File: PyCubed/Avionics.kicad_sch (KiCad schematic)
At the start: 37 parts, among them J19 F3311A7H121014E200, J8 Conn_01x09, U1 MAX706RESA, U2 ATSAMD51J19A-AU, U3 BMX160, Y1 32.768kHz

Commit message: PyCubed Schematic Finalized
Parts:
- added C61: 0.1uF, Capacitor_SMD:C_0603_1608Metric, symbol mainboard:C_Small
- added IC3: UA741IDT, SOIC127P600X175-8N, symbol SamacSys_Parts:UA741IDT
- added JP3, JP4: SolderJumper_2_Open, Jumper:SolderJumper-2_P1.3mm_Open_Pad1.0x1.5mm, symbol Jumper:SolderJumper_2_Open
- added R139, R140, R141, R143, R145: 10K, Resistor_SMD:R_0603_1608Metric, symbol Device:R_US
- added R144: ERA-8PEB6803V, ERA8P, symbol SamacSys_Parts:ERA-8PEB6803V
- added R30 (x2): 100K, Resistor_SMD:R_0603_1608Metric, symbol Device:R_US
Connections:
- net 3.3V: now also IC3.7 (VCC+), R139.1, R145.2
- net AIN5: now also C61.1, IC3.6 (OUTPUT), R144.2
- net GND: now also J19.MP1, J19.MP2, IC3.4 (VCC-), R140.2, R143.2; no longer J19.10
- net PB07: now also J19.12
- net PB09: now also J19.13
- net PB14: now also J19.14
- net RX: now also JP3.1 (A)
- net TX: now also JP4.1 (A)
- net at J19.11: now also JP3.2 (B)
- new net: C61.2, IC3.2 (INVERTING_INPUT), R144.1, R30.1
- new net: IC3.3 (NON-INVERTING_INPUT), R143.1, R30.1
- new net: J19.10, JP4.2 (B)
- new net: R139.2, R140.1, R30.2
- new net: R141.1, R145.1
- new net BAT_THERM: R141.2, R30.2

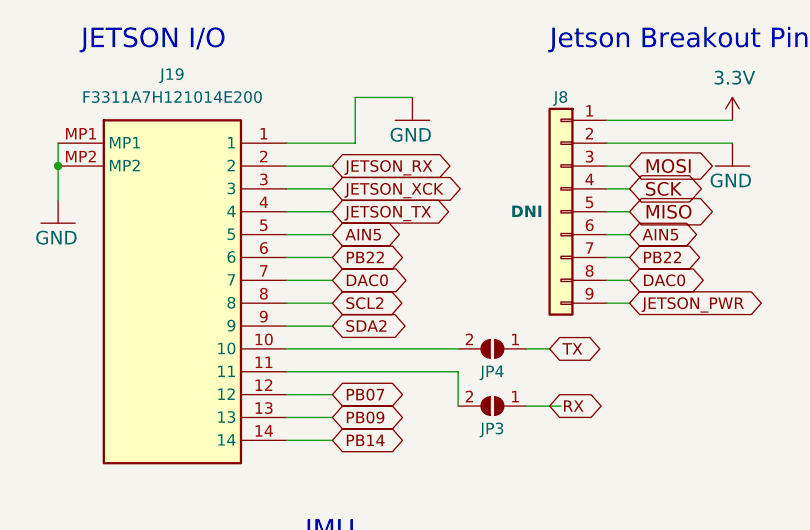
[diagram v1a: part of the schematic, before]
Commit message: PyCubed Interface Connectors Placed
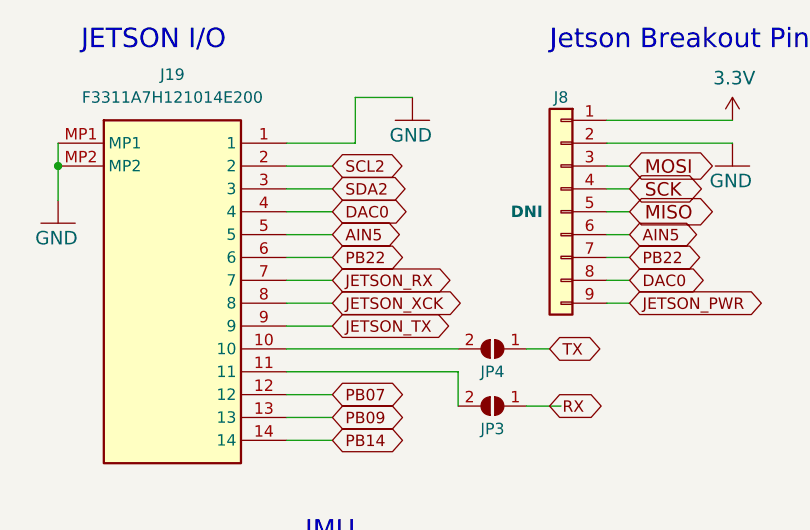
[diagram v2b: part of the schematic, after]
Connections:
- net DAC0: now also J19.4; no longer J19.7
- net JETSON_RX: now also J19.7; no longer J19.2
- net JETSON_TX: now also J19.9; no longer J19.4
- net JETSON_XCK: now also J19.8; no longer J19.3
- net SCL2: now also J19.2; no longer J19.8
- net SDA2: now also J19.3; no longer J19.9
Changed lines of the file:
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@@
     (effects (font (size 1.4986 1.4986)) (justify left bottom))
   )
-  (global_label "SDA2" (shape bidirectional) (at 218.44 57.15 0)
-    (effects (font (size 1.27 1.27)) (justify left))
-    (property "Intersheetrefs" "${INTERSHEET_REFS}" (at 218.44 57.15 0)
-      (effects (font (size 1.27 1.27)) hide)
-    )
-  )
   (global_label "ENAB_BURN1" (shape bidirectional) (at 127 161.29 0)
     (effects (font (size 1.27 1.27)) (justify left))
@@
     )
   )
+  (global_label "JETSON_XCK" (shape bidirectional) (at 218.44 54.61 0)
+    (effects (font (size 1.27 1.27)) (justify left))
+    (property "Intersheetrefs" "${INTERSHEET_REFS}" (at 218.44 54.61 0)
+      (effects (font (size 1.27 1.27)) hide)
+    )
+  )
   (global_label "PB09" (shape bidirectional) (at 127 130.81 0)
     (effects (font (size 1.27 1.27)) (justify left))
@@
     (effects (font (size 1.27 1.27)) (justify left))
     (property "Intersheetrefs" "${INTERSHEET_REFS}" (at 160.02 140.97 0)
+      (effects (font (size 1.27 1.27)) hide)
+    )
+  )
+  (global_label "SDA2" (shape bidirectional) (at 218.44 41.91 0)
+    (effects (font (size 1.27 1.27)) (justify left))
+    (property "Intersheetrefs" "${INTERSHEET_REFS}" (at 218.44 41.91 0)
       (effects (font (size 1.27 1.27)) hide)
     )
@@
     )
   )
-  (global_label "JETSON_TX" (shape bidirectional) (at 218.44 44.45 0)
-    (effects (font (size 1.27 1.27)) (justify left))
-    (property "Intersheetrefs" "${INTERSHEET_REFS}" (at 218.44 44.45 0)
-      (effects (font (size 1.27 1.27)) hide)
-    )
-  )
   (global_label "FLASH_IO2" (shape bidirectional) (at 88.9 130.81 180)
     (effects (font (size 1.27 1.27)) (justify right))
@@
     )
   )
+  (global_label "DAC0" (shape bidirectional) (at 218.44 44.45 0)
+    (effects (font (size 1.27 1.27)) (justify left))
+    (property "Intersheetrefs" "${INTERSHEET_REFS}" (at 218.44 44.45 0)
+      (effects (font (size 1.27 1.27)) hide)
+    )
+  )
   (global_label "JETSON_PWR" (shape bidirectional) (at 251.46 54.61 0)
     (effects (font (size 1.27 1.27)) (justify left))
@@
     (effects (font (size 1.27 1.27)) (justify right))
     (property "Intersheetrefs" "${INTERSHEET_REFS}" (at 90.17 172.72 0)
-      (effects (font (size 1.27 1.27)) hide)
-    )
-  )
-  (global_label "DAC0" (shape bidirectional) (at 218.44 52.07 0)
-    (effects (font (size 1.27 1.27)) (justify left))
-    (property "Intersheetrefs" "${INTERSHEET_REFS}" (at 218.44 52.07 0)
       (effects (font (size 1.27 1.27)) hide)
     )
@@
     )
   )
+  (global_label "SCL2" (shape bidirectional) (at 218.44 39.37 0)
+    (effects (font (size 1.27 1.27)) (justify left))
+    (property "Intersheetrefs" "${INTERSHEET_REFS}" (at 218.44 39.37 0)
+      (effects (font (size 1.27 1.27)) hide)
+    )
+  )
   (global_label "PB22" (shape bidirectional) (at 251.46 49.53 0)
     (effects (font (size 1.27 1.27)) (justify left))
@@
     )
   )
+  (global_label "JETSON_RX" (shape bidirectional) (at 218.44 52.07 0)
+    (effects (font (size 1.27 1.27)) (justify left))
+    (property "Intersheetrefs" "${INTERSHEET_REFS}" (at 218.44 52.07 0)
+      (effects (font (size 1.27 1.27)) hide)
+    )
+  )
   (global_label "AIN5" (shape bidirectional) (at 274.32 139.7 0)
     (effects (font (size 1.27 1.27)) (justify left))
@@
     )
   )
-  (global_label "JETSON_RX" (shape bidirectional) (at 218.44 39.37 0)
-    (effects (font (size 1.27 1.27)) (justify left))
-    (property "Intersheetrefs" "${INTERSHEET_REFS}" (at 218.44 39.37 0)
-      (effects (font (size 1.27 1.27)) hide)
-    )
-  )
   (global_label "VBUS_RESET" (shape output) (at 90.17 156.21 180)
     (effects (font (size 1.27 1.27)) (justify right))
@@
     )
   )
-  (global_label "JETSON_XCK" (shape bidirectional) (at 218.44 41.91 0)
-    (effects (font (size 1.27 1.27)) (justify left))
-    (property "Intersheetrefs" "${INTERSHEET_REFS}" (at 218.44 41.91 0)
-      (effects (font (size 1.27 1.27)) hide)
-    )
-  )
   (global_label "AIN5" (shape bidirectional) (at 251.46 46.99 0)
     (effects (font (size 1.27 1.27)) (justify left))
@@
     )
   )
-  (global_label "SCL2" (shape bidirectional) (at 218.44 54.61 0)
-    (effects (font (size 1.27 1.27)) (justify left))
-    (property "Intersheetrefs" "${INTERSHEET_REFS}" (at 218.44 54.61 0)
-      (effects (font (size 1.27 1.27)) hide)
-    )
-  )
   (global_label "PB07" (shape bidirectional) (at 127 125.73 0)
     (effects (font (size 1.27 1.27)) (justify left))
@@
       (effects (font (size 1.27 1.27)) hide)
     )
+  )
+  (global_label "JETSON_TX" (shape bidirectional) (at 218.44 57.15 0)
+    (effects (font (size 1.27 1.27)) (justify left))
+    (property "Intersheetrefs" "${INTERSHEET_REFS}" (at 218.44 57.15 0)
+      (effects (font (size 1.27 1.27)) hide)
+    )

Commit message: PyCubed Routing Done
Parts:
- removed J8: Conn_01x09, Connector_PinHeader_2.54mm:PinHeader_1x09_P2.54mm_Vertical, symbol Connector_Generic:Conn_01x09
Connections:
- net AIN5: no longer J19.5
- net BURN_RELAY_A: now also U2.10 (PB07); no longer U2.28 (PB15)
- net DAC0: now also J19.13; no longer J19.4
- net ENAB_BURN2: now also U2.12 (PB09); no longer U2.32 (PA15)
- net ENAB_BURN3: now also U2.13 (PA04); no longer U2.39 (PB16)
- net ENAB_BURN4: now also U2.27 (PB14); no longer U2.40 (PB17)
- net ENAB_IMU: now also U2.39 (PB16); no longer U2.9 (PB06)
- net ENAB_RF: now also U2.9 (PB06); no longer U2.13 (PA04)
- net GND: now also J19.14
- net JETSON_RX: now also J19.8; no longer J19.7
- net JETSON_TX: now also J19.6; no longer J19.9
- net JETSON_XCK: now also J19.7; no longer J19.8
- net PB09: now also J19.9, U2.28 (PB15); no longer J19.13, U2.12 (PB09)
- net PB22: now also J19.5; no longer J19.6
- net at JP4.2 (B): now also J19.11; no longer J19.10
- net at JP3.2 (B): now also J19.12; no longer J19.11
- removed net PB07: J19.12, U2.10 (PB07)
- removed net PB14: J19.14, U2.27 (PB14)
- new net ENAB_JET: U2.40 (PB17)
- new net PA15: U2.32 (PA15)
- no-connect marks 6 -> 8
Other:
- note removed: "Jetson Breakout Pins"

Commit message: Mainboard Final Design
Updated BMS
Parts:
- removed C61: 0.1uF, Capacitor_SMD:C_0603_1608Metric, symbol mainboard:C_Small
- removed H1, H2, H3, H4: MountingHole_Pad, MountingHole:MountingHole_3.2mm_M3_DIN965_Pad, symbol Mechanical:MountingHole_Pad
- removed IC3: UA741IDT, SOIC127P600X175-8N, symbol SamacSys_Parts:UA741IDT
- removed R139, R140, R143, R145: 10K, Resistor_SMD:R_0603_1608Metric, symbol Device:R_US
- removed R144: ERA-8PEB6803V, ERA8P, symbol SamacSys_Parts:ERA-8PEB6803V
- removed R30 (x2): 100K, Resistor_SMD:R_0603_1608Metric, symbol Device:R_US
- removed R42: 10k, Resistor_SMD:R_0603_1608Metric, symbol Device:R_US
- removed U1: MAX706RESA, Package_SO:SO-8_3.9x4.9mm_P1.27mm, symbol mainboard:MAX708RESA-T
- added C13: 0.1uF, Capacitor_SMD:C_0603_1608Metric, symbol Device:C_Small
- added JP3 (x4): SolderJumper_2_Open, Jumper:SolderJumper-2_P1.3mm_Open_Pad1.0x1.5mm, symbol Jumper:SolderJumper_2_Open
- added Q19: IRLML2803, Package_TO_SOT_SMD:SOT-23, symbol Transistor_FET:IRLML2060
- added R13: 0R, Resistor_SMD:R_0603_1608Metric, symbol Device:R_US
- added R54, R56: 10K, Resistor_SMD:R_0603_1608Metric, symbol Device:R_US
- added R92: DNI (0R), Resistor_SMD:R_0603_1608Metric, symbol Device:R_US
- added R93: 200K, Resistor_SMD:R_0603_1608Metric, symbol Device:R_US
- added U2: MAX706RESA+, Package_SO:SOIC-8_3.9x4.9mm_P1.27mm, symbol mainboard:MAX708RESA+
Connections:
- net 3.3V: now also R141.1, C13.1, R54.1, R56.1, U2.2 (VCC)
- net AIN5: now also J19.10, JP3.1 (A)
- net BAT_THERM: now also JP3.1 (A), JP3.2 (B), JP3.2 (B); no longer R141.2
- net DAC0: now also J19.2; no longer J19.13
- net GND: now also C13.2, R93.2, U2.3 (GND), U2.4 (PFI)
- net JETSON_RX: now also J19.7; no longer J19.8
- net JETSON_TX: now also J19.9; no longer J19.6
- net JETSON_XCK: now also J19.8; no longer J19.7
- net SCL2: now also R56.2; no longer J19.2
- net SDA2: now also R54.2; no longer J19.3
- net WDT_WDI: now also U2.6 (~{WDI})
- net ~{RESET}: now also Q19.3 (D), R92.1
- net at JP3.2 (B): now also J19.3; no longer J19.12
- net at JP4.2 (B): now also J19.4; no longer J19.11
- net PB09 renamed STAT1
- net STAT1: no longer J19.9
- net PB22: no longer names the net of J19.5
- net PB22: no longer U2.49 (PB22)
- net ~{CHRG} renamed INOKB
- new net: JP3.2 (B), JP3.2 (B), R141.2
- new net: U2.1 (~{MR}), U2.8 (~{WDO})
- new net: R13.2, U2.7 (~{RESET})
- new net: Q19.2 (S), R13.1, R92.2
- new net SCL2_JETSON: J19.13
- new net SDA2_JETSON: J19.12
- new net THM: JP3.1 (A)
- new net TS: JP3.1 (A)
- new net WDT_EN: Q19.1 (G), R93.1, U2.49 (PB22)
- no-connect marks 8 -> 9
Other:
- note added: "BATTERY BOARD THERMAL"
- note added: "USB Charge Controller BQ25883 has a battery thermal input. These jumpers configure where input thermistor will get connected. Solder JP6 and JP12 to connect the input to the MCU. Solder JP11 to connect the input to the USB CHARGE IC. Solder JP11 to connect the input to the SOLAR CHARGE IC."
- note added: "WDT able to reset MCU when WDT_EN is high"
- note removed: "Mounting Holes"
- note removed: "WDT enabled when installed"
- moved on the sheet: C7, C9, J19, JP3, JP4, R141, R41, U3
